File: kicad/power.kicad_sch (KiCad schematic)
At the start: 21 parts, among them U1 HT7533-1, U2 TLV62569DBV, U3 MCP6001T-E/OT

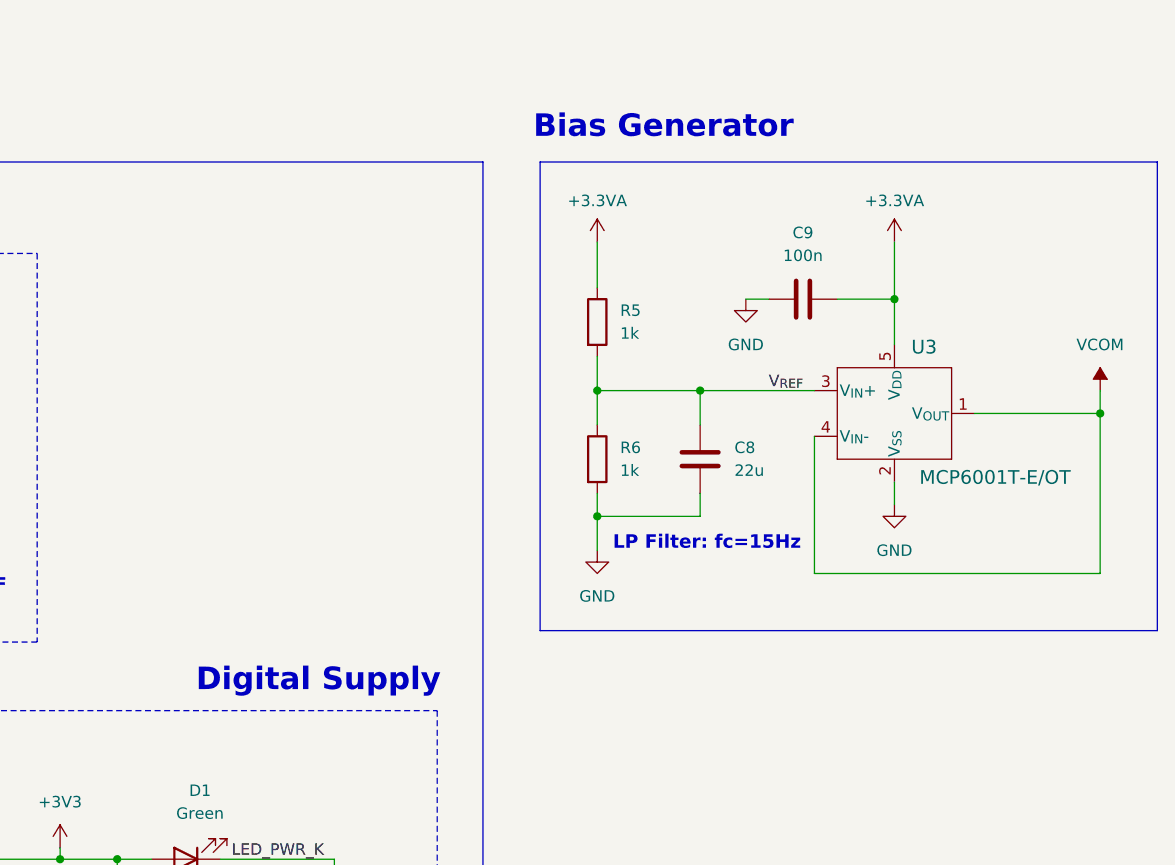
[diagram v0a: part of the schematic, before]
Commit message: removed custom library for MCP6001 OpAmp
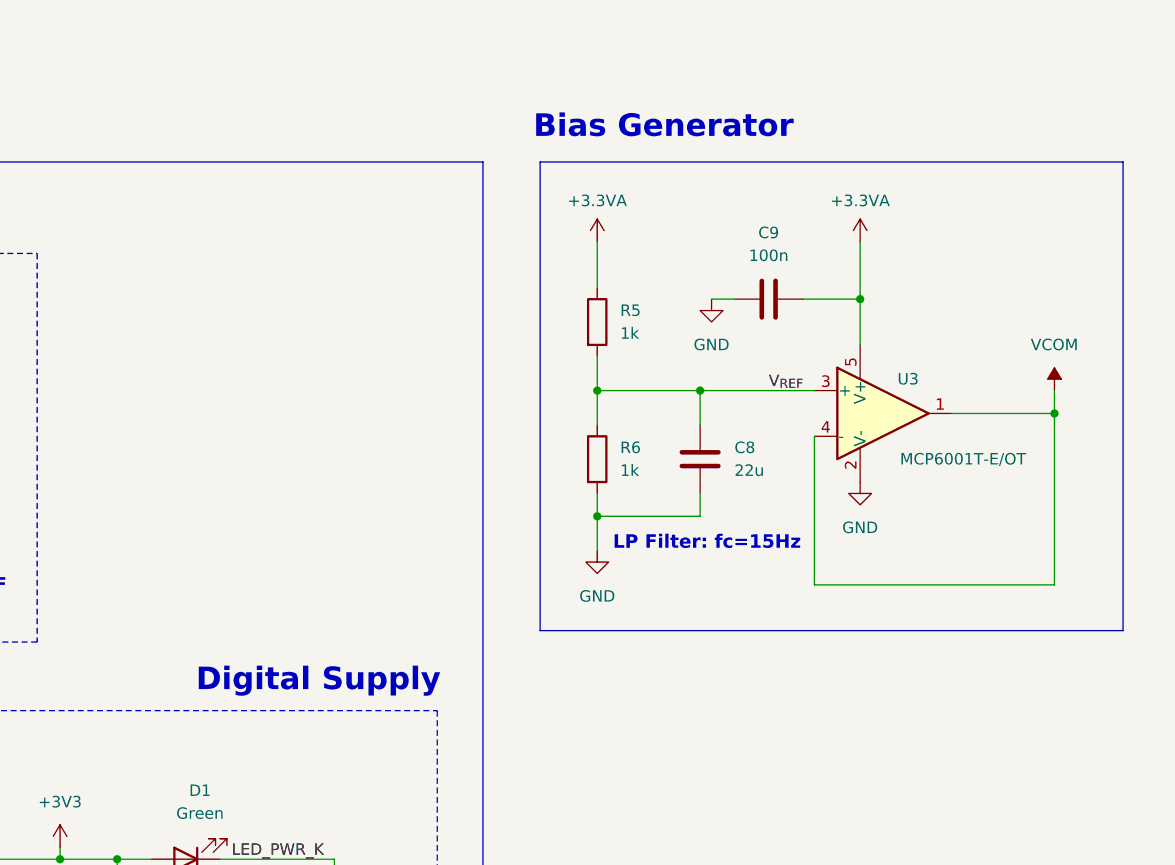
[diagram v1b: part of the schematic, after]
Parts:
- removed U3: MCP6001T-E/OT, SOT-23-5_MC_MCH, symbol bias_generator_microchip:MCP6001T-E_OT
- added U3: MCP6001T-E/OT, Package_TO_SOT_SMD:SOT-23-5, symbol Amplifier_Operational:MCP6001-OT
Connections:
- net +3.3VA: now also U3.5 (V+)
- net GND: now also U3.2 (V-)
- net VCOM: now also U3.1, U3.4 (-)
- net V_{REF}: now also U3.3 (+)
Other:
- moved on the sheet: C9

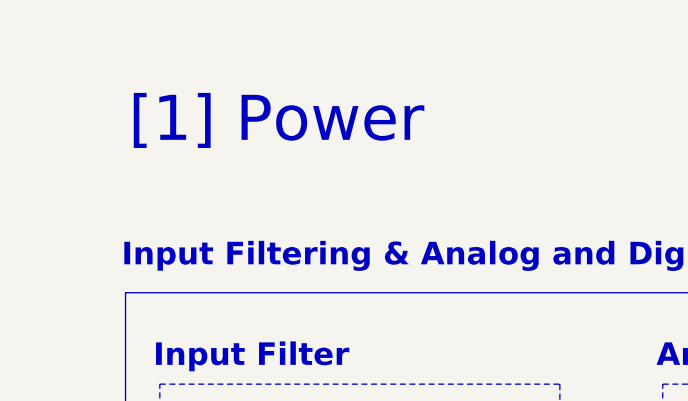
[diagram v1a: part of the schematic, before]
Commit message: Added schematic for MCU
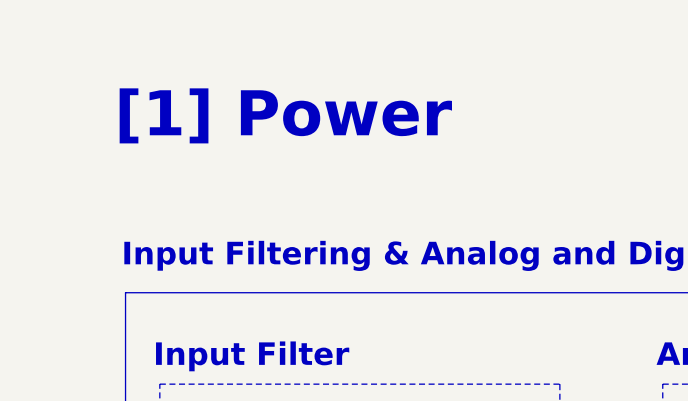
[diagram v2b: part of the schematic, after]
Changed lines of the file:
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@@
 	(text "[1] Power"
 		(exclude_from_sim no)
-		(at 42.164 21.59 0)
+		(at 42.926 21.082 0)
 		(effects
 			(font
 				(size 5 5)
-				(thickness 0.625)
+				(thickness 1.2)
+				(bold yes)
 			)
 		)

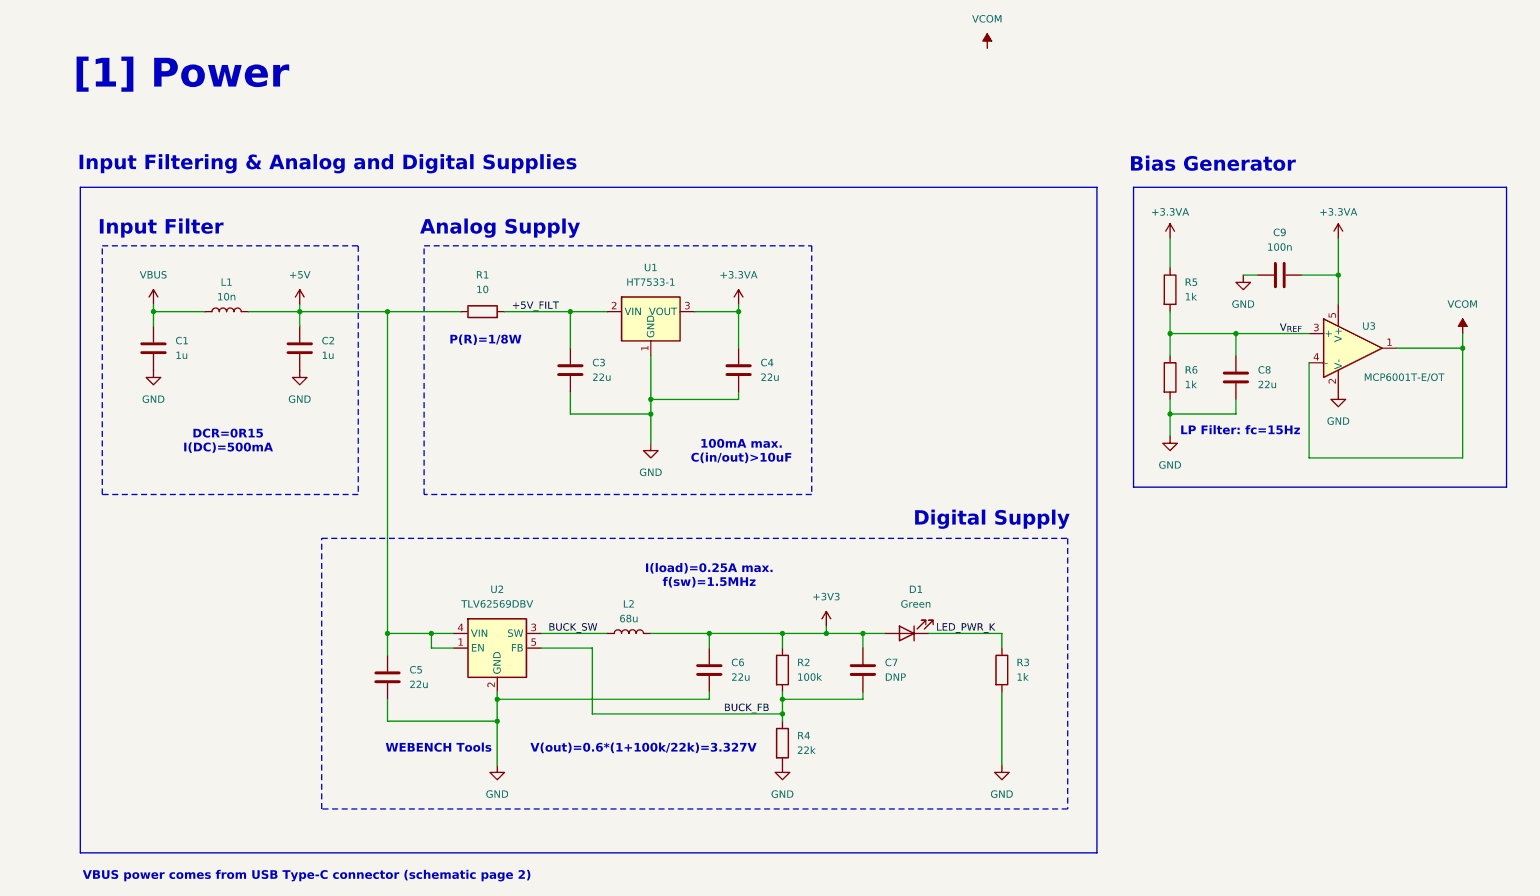
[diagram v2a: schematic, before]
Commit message: Updated parts numbering and notes
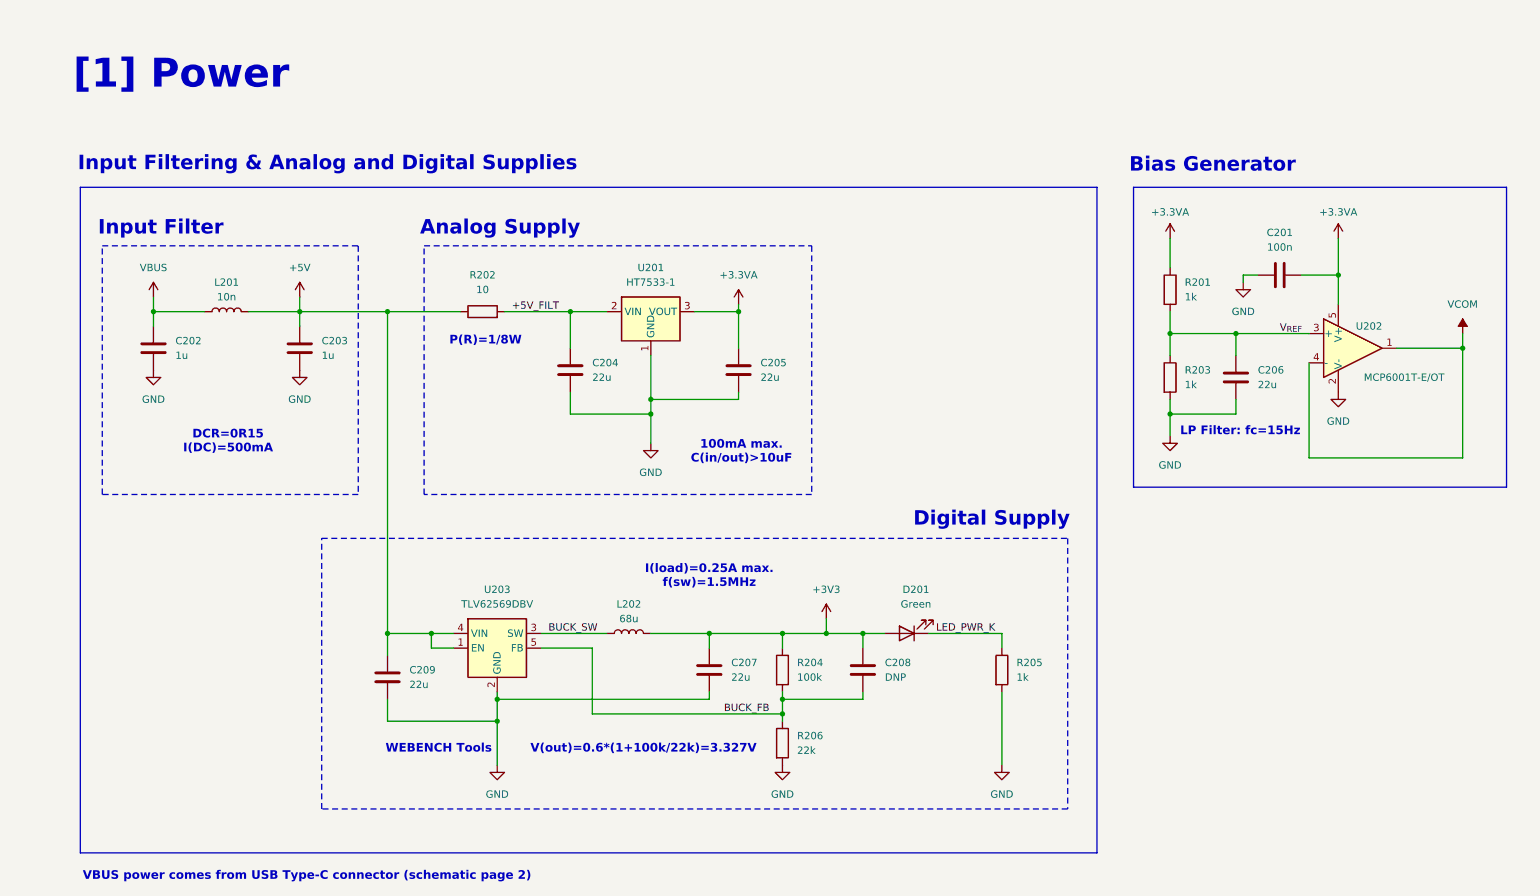
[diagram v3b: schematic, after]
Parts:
- renumbered C9 to C201, C1 to C202, C2 to C203, C3 to C204, C4 to C205, C8 to C206, C6 to C207, C7 to C208, C5 to C209, D1 to D201, L1 to L201, L2 to L202, R5 to R201, R1 to R202, R6 to R203, R2 to R204, R3 to R205, R4 to R206, U1 to U201, U3 to U202, U2 to U203

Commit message: Save Progress
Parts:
- C201, C208: footprint (none) -> Capacitor_SMD:C_0402_1005Metric
- C202, C203: footprint (none) -> Capacitor_SMD:C_0603_1608Metric
- C204, C205, C206, C207, C209: footprint (none) -> Capacitor_SMD:C_0805_2012Metric
- D201: footprint (none) -> LED_SMD:LED_0603_1608Metric
- L201: footprint (none) -> Inductor_SMD:L_0402_1005Metric
- R201, R203, R204, R205, R206: footprint (none) -> Resistor_SMD:R_0402_1005Metric
- R202: value 10 -> 10R; footprint (none) -> Resistor_SMD:R_0805_2012Metric
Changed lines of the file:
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@@
 			)
 		)
-		(property "Footprint" ""
+		(property "Footprint" "Capacitor_SMD:C_0805_2012Metric"
 			(at 111.4552 76.2 0)
 			(effects
@@
 			)
 		)
-		(property "Footprint" ""
+		(property "Footprint" "Capacitor_SMD:C_0805_2012Metric"
 			(at 140.6652 76.2 0)
 			(effects
@@
 			)
 		)
-		(property "Footprint" ""
+		(property "Footprint" "Capacitor_SMD:C_0402_1005Metric"
 			(at 162.2552 128.27 0)
 			(effects
@@
 			)
 		)
-		(property "Value" "10"
+		(property "Value" "10R"
 			(at 95.25 58.42 90)
 			(effects
@@
 			)
 		)
-		(property "Footprint" ""
+		(property "Footprint" "Resistor_SMD:R_0805_2012Metric"
 			(at 95.25 64.008 90)
 			(effects
@@
 			)
 		)
-		(property "Footprint" ""
+		(property "Footprint" "LED_SMD:LED_0603_1608Metric"
 			(at 168.91 118.11 0)
 			(effects
@@
 			)
 		)
-		(property "Footprint" ""
+		(property "Footprint" "Capacitor_SMD:C_0402_1005Metric"
 			(at 237.49 54.9148 0)
 			(effects
@@
 			)
 		)
-		(property "Footprint" ""
+		(property "Footprint" "Resistor_SMD:R_0402_1005Metric"
 			(at 212.852 58.42 90)
 			(effects
@@
 			)
 		)
-		(property "Footprint" ""
+		(property "Footprint" "Capacitor_SMD:C_0805_2012Metric"
 			(at 227.0252 77.47 0)
 			(effects
@@
 			)
 		)
-		(property "Footprint" ""
+		(property "Footprint" "Resistor_SMD:R_0402_1005Metric"
 			(at 145.542 137.16 90)
 			(effects
@@
 			)
 		)
-		(property "Footprint" ""
+		(property "Footprint" "Capacitor_SMD:C_0603_1608Metric"
 			(at 39.0652 72.39 0)
 			(effects
@@
 			)
 		)
-		(property "Footprint" ""
+		(property "Footprint" "Resistor_SMD:R_0402_1005Metric"
 			(at 212.852 73.66 90)
 			(effects
@@
 			)
 		)
-		(property "Footprint" ""
+		(property "Footprint" "Resistor_SMD:R_0402_1005Metric"
 			(at 145.542 124.46 90)
 			(effects
@@
 			)
 		)
-		(property "Footprint" ""
+		(property "Footprint" "Inductor_SMD:L_0402_1005Metric"
 			(at 50.8 62.23 0)
 			(effects
@@
 			)
 		)
-		(property "Footprint" ""
+		(property "Footprint" "Capacitor_SMD:C_0603_1608Metric"
 			(at 64.4652 72.39 0)
 			(effects
@@
 			)
 		)
-		(property "Footprint" ""
+		(property "Footprint" "Capacitor_SMD:C_0805_2012Metric"
 			(at 135.5852 128.27 0)
 			(effects
@@
 			)
 		)
-		(property "Footprint" ""
+		(property "Footprint" "Capacitor_SMD:C_0805_2012Metric"
 			(at 77.7748 121.92 0)
 			(effects
@@
 			)
 		)
-		(property "Footprint" ""
+		(property "Footprint" "Resistor_SMD:R_0402_1005Metric"
 			(at 183.642 124.46 90)
 			(effects
